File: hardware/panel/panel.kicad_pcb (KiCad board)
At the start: 2 copper layers, 40.2 x 128.4 mm, 3 parts

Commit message: Update panel
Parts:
- removed the G*** at (0.00, 0.00) (x3)
- added  : , panel:MountingHoleEurorackSlotM3, F.Cu at (-12.6, -61.2)
- added  : , panel:MountingHoleEurorackSlotM3, F.Cu at (-12.6, 61.2)
- added G*** (x3): LOGO, LOGO, F.Cu at (0.00, 0.00)
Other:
- board size 40.2 x 128.4 mm -> 40.3 x 128.5 mm

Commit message: Update panel
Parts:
- removed the G*** at (0.00, 0.00) (x3)
- added G*** (x3): LOGO, LOGO, F.Cu at (0.00, 0.00)
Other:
- outline, holes or cut-outs redrawn

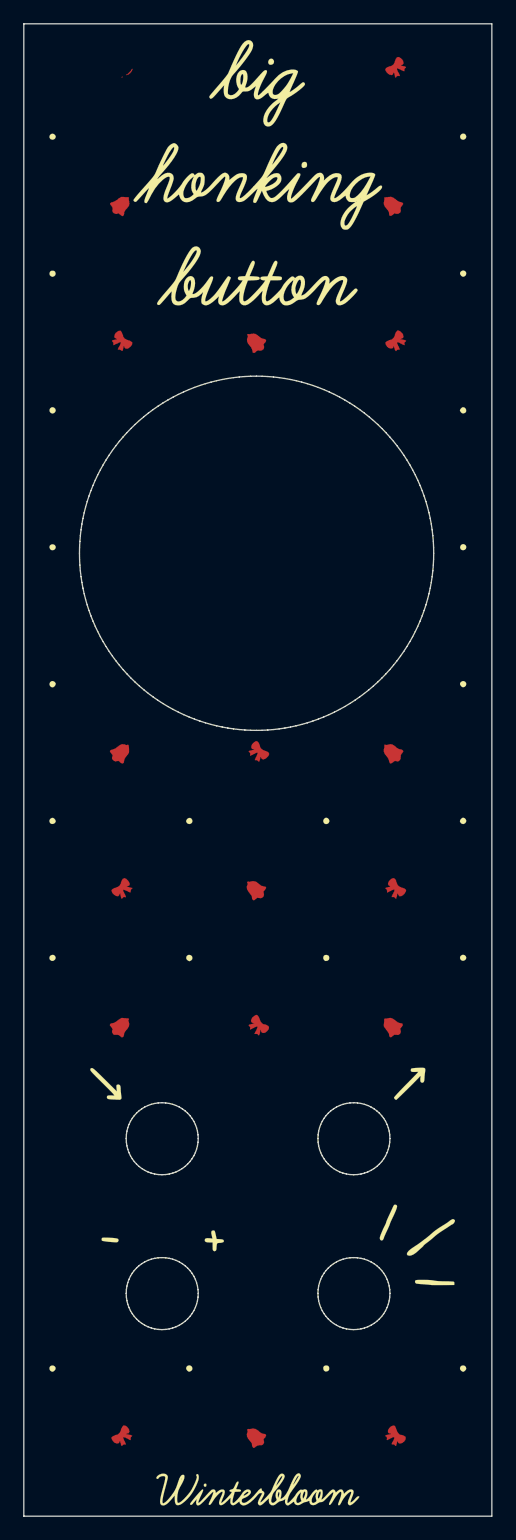
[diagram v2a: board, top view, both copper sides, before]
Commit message: Update panel with new logo
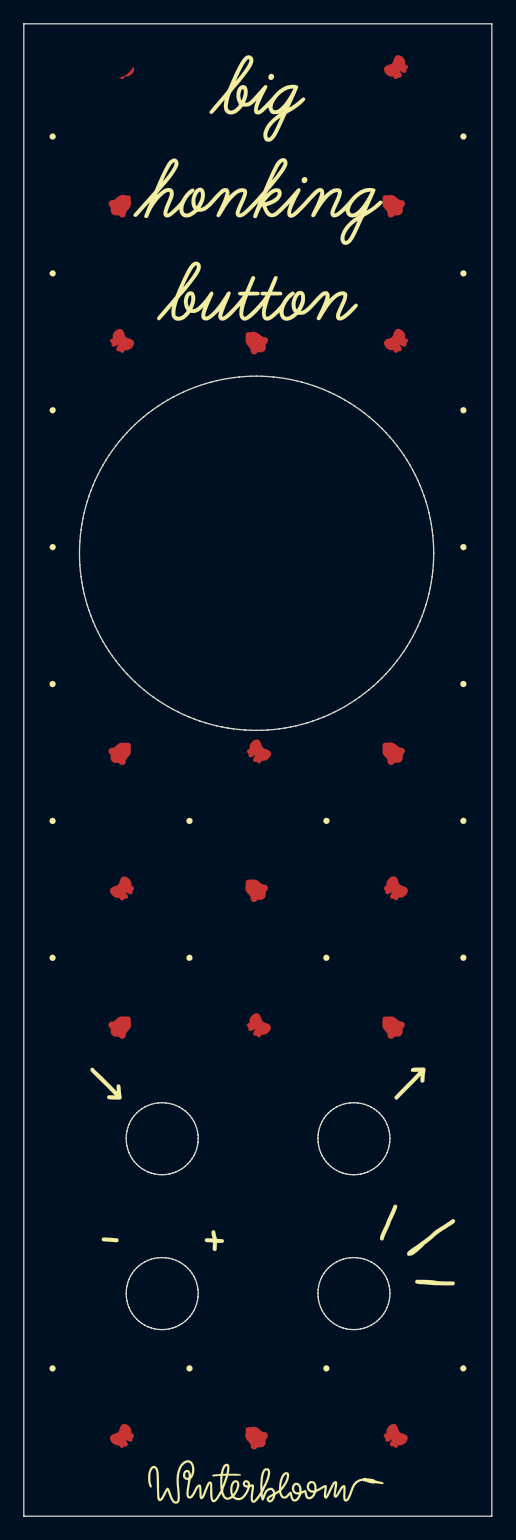
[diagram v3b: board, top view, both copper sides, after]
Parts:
- removed the G*** at (0.00, 0.00) (x3)
- added G*** (x3): LOGO, LOGO, F.Cu at (0.00, 0.00)

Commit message: Make panel reversable
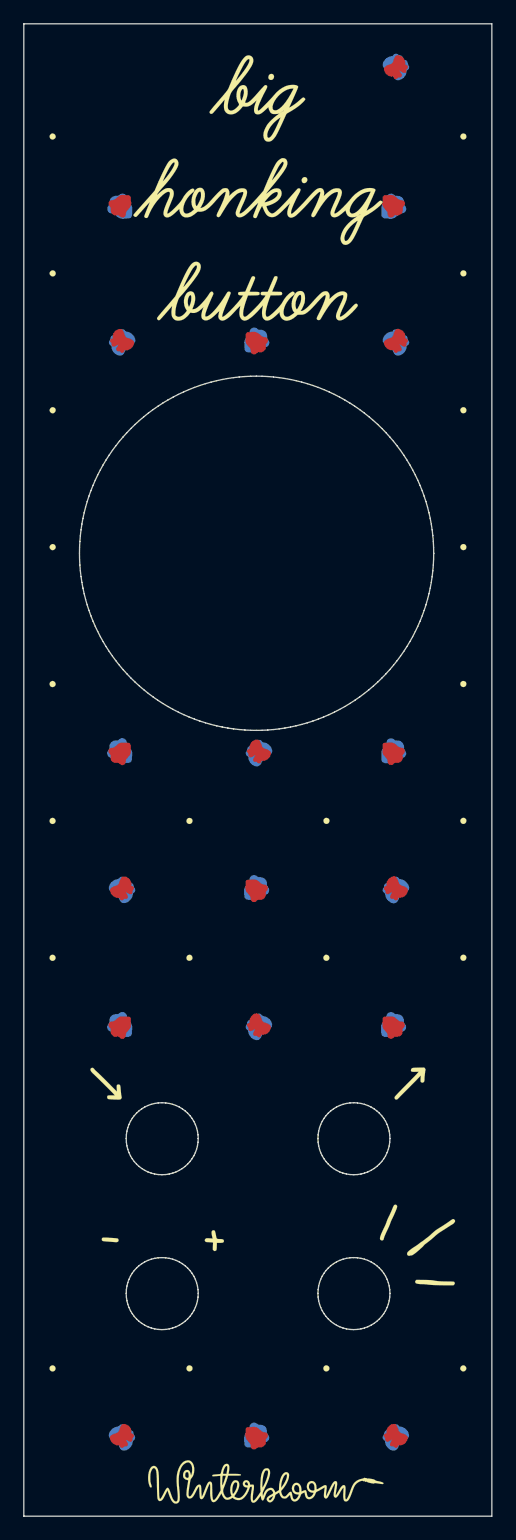
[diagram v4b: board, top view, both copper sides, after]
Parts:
- removed the G*** at (0.00, 0.00) (x3)
- added G*** (x6): LOGO, LOGO, F.Cu at (0.00, 0.00)
